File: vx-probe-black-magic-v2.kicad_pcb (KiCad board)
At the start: 2 copper layers, 72.4 x 41.9 mm, 52 parts, among them P1 USB MINI B, P10 CONN_01X01, P11 CONN_01X09, P12 CONN_01X03, P2 +5v power input, P3 +5v external input, P4 CONN_02X05, P5 CONN_01X04, P6 swdio/jtag, P7 CONN_01X01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

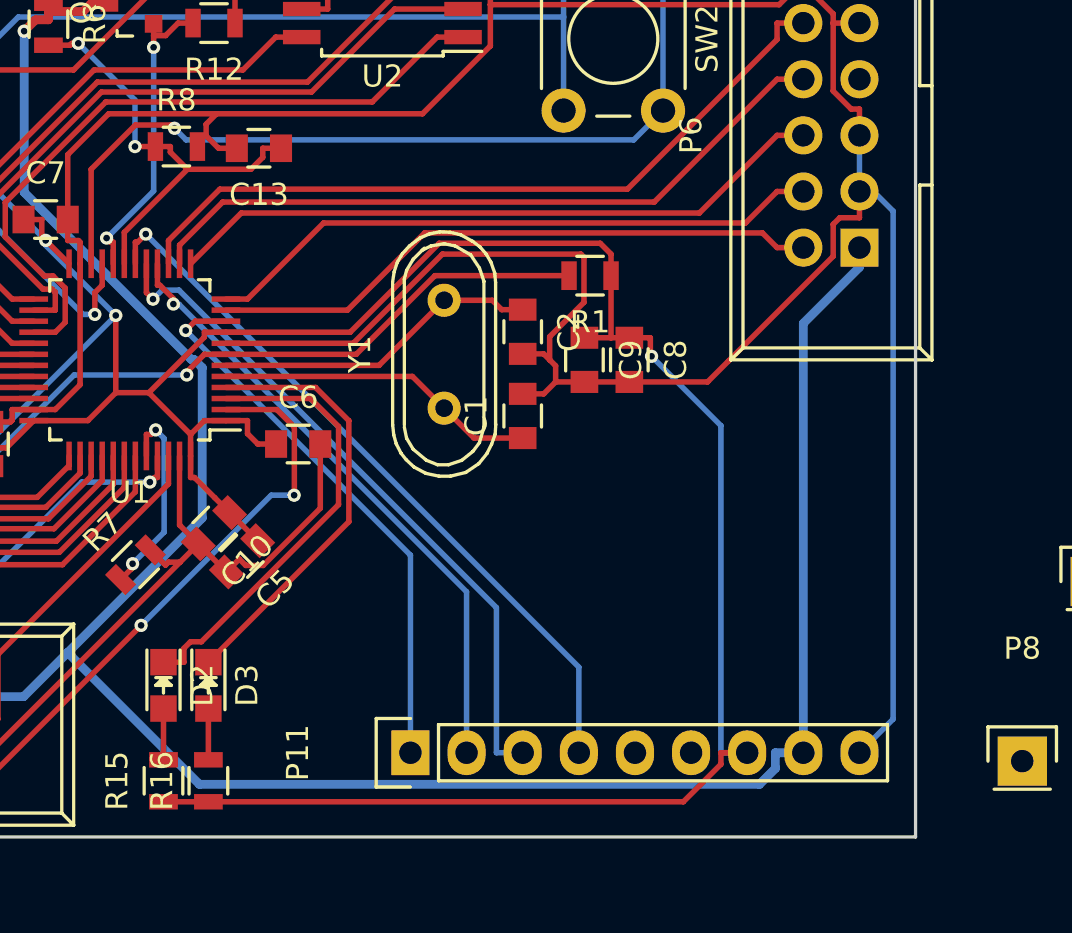
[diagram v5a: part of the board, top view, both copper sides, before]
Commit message: rerouted the extension connector
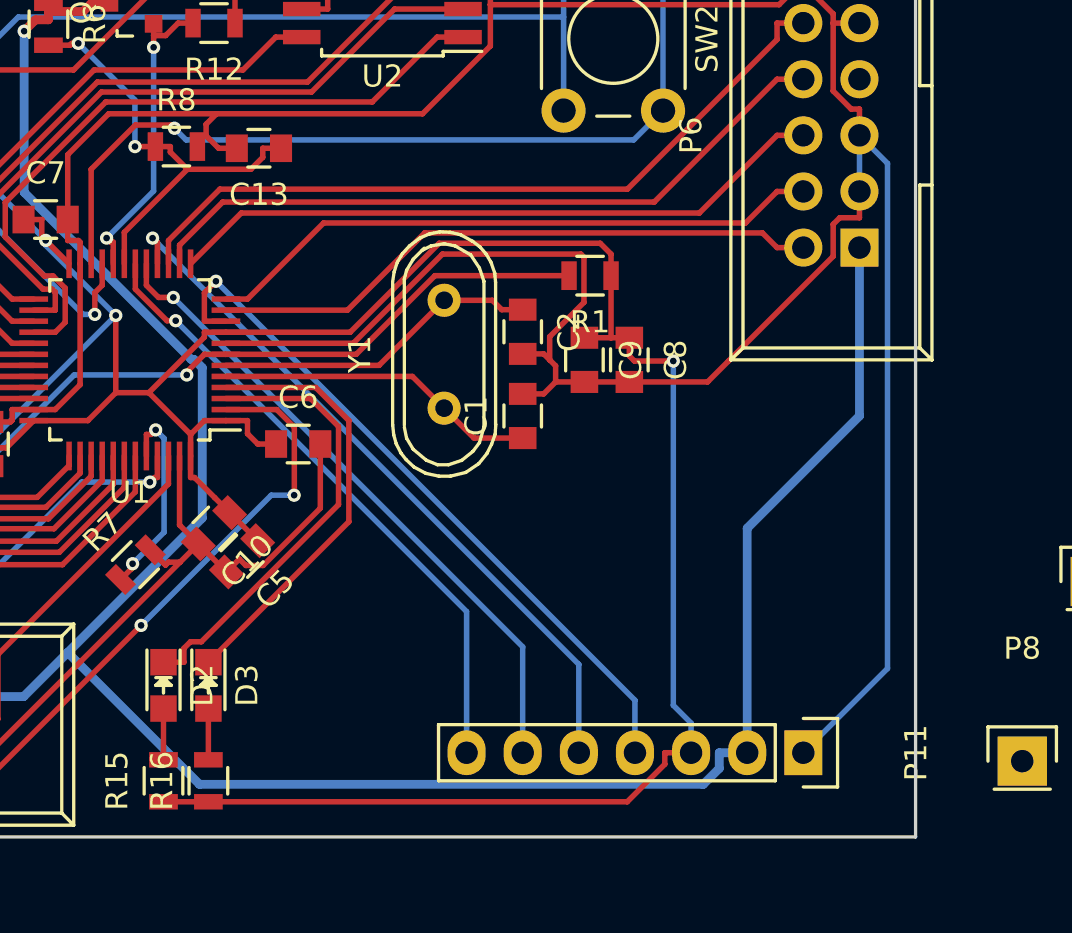
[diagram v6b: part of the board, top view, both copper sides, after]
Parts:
- P11: value CONN_01X09 -> CONN_01X07; footprint Pin_Headers:Pin_Header_Straight_1x09 -> Pin_Headers:Pin_Header_Straight_1x07
- moved P11 17.8 mm to (114.3, 77.5), turned to 270 degrees
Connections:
- P11 pad 1: /x4 -> GND
- P11 pad 2: /x5 -> /TPWR
- P11 pad 3: /x6 -> +3V3
- P11 pad 4: /x7 -> /x4
- P11 pad 5: /x2 -> /x5
- P11 pad 6: /x3 -> /x6
- P11 pad 7: +3V3 -> /x7
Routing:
- net /x4: track 25.3 -> 32.2 mm
- net /x7: track 33.2 -> 28.6 mm
- net /x5: track 28.1 -> 32.6 mm
- net +3V3: track 171.6 -> 167.8 mm
- net GND: track 344.9 -> 348.6 mm
- net /x6: track 31.1 -> 29.6 mm
- net /TPWR: track 105.4 -> 103.9 mm

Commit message: renamed extension connector signals
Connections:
- net /x5 renamed /x2
- net /x6 renamed /x3
- P11 pad 4: /x4 -> /x1
- P11 pad 7: /x7 -> /x4
- U1 pad 10: /x4 -> /x1
- U1 pad 18: /x7 -> /x4
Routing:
- net /x1: track 0.00 -> 32.2 mm, vias 0 -> 1
- net /x7: track 28.6 -> 0.00 mm, vias 1 -> 0
- net /x4: track 32.2 -> 28.6 mm

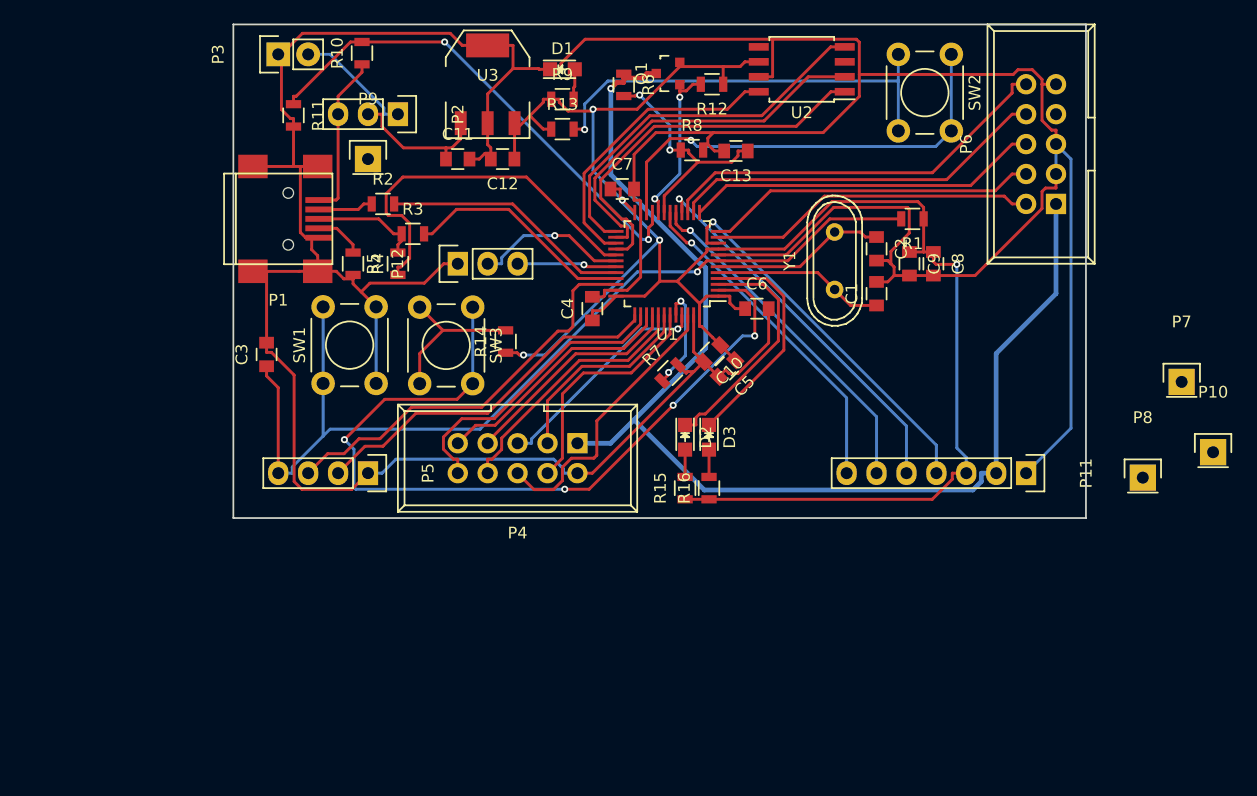
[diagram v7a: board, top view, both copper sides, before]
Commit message: rerouted many pins because of pc13-pc15 output driving limitations
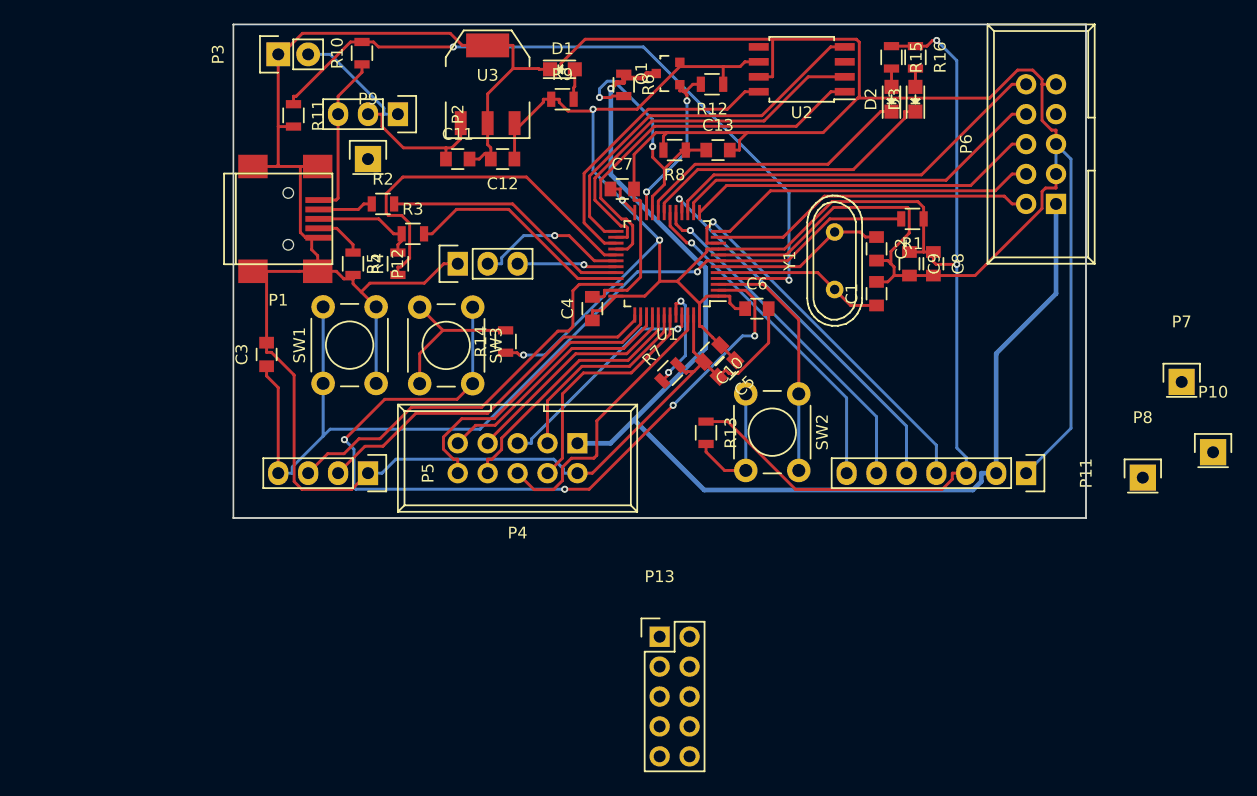
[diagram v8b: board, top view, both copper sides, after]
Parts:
- added P13: CONN_02X04, Pin_Headers:Pin_Header_Straight_2x05, F.Cu at (83.2, 91.4)
- moved R15 40.6 mm to (102.9, 42.2), turned to 270 degrees
- moved R16 40.6 mm to (104.9, 42.2), turned to 270 degrees
- moved D2 33.6 mm to (102.9, 45.7), turned to 90 degrees
- moved D3 33.6 mm to (104.9, 45.7), turned to 90 degrees
- moved SW2 31.6 mm to (95.0, 70.7)
- moved R13 28.5 mm to (87.1, 74.0), turned to 270 degrees
- moved C13 1.53 mm to (88.1, 50.0), turned to 0 degrees
- moved R8 1.47 mm to (84.5, 50.0), turned to 180 degrees
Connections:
- U1 pad 19: /TPWR_IN -> /LED2
- U1 pad 20: /TPWR_CTRL -> /LED1
- U1 pad 21: /VUSB -> /TPWR_IN
- U1 pad 22: /BTN1 -> /TPWR_CTRL
- U1 pad 3: /LED1 -> /BTN1
- U1 pad 4: /LED2 -> /VUSB
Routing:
- net Net-(R13-Pad2): track 37.1 -> 11.2 mm, vias 1 -> 0
- net +3V3: track 167.8 -> 189.5 mm, vias 5 -> 6
- net /VUSB: track 42.1 -> 63.4 mm
- net /BTN1: track 38.3 -> 20.9 mm, vias 1 -> 0
- net /LED2: track 19.7 -> 25.7 mm
- net /LED1: track 20.4 -> 23.9 mm
- net GND: track 348.6 -> 350.8 mm
- net /TPWR_IN: track 20.4 -> 22.5 mm
- net Net-(D3-Pad2): track 2.32 -> 1.56 mm
- net Net-(D2-Pad2): track 2.32 -> 1.56 mm
